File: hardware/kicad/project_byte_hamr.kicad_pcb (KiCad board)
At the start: 4 copper layers, 125.5 x 80.3 mm, 95 parts, among them J2 Conn_01x13_Socket, J3 Bus_Apple_II_Card_Side, J4 CONN_02X03, U1 LFE5U-25F-6BG381C, U10 IS25LP128F-JBLE, U11 SN74LVC8T245, U12 SN74LVC8T245, U13 SN74LVC8T245, U14 SN74LVC8T245, U2 MT48LC16M16A2TG, U3 TLV62569DBV, U4 TLV62569DBV, U5 TLV62569DBV, U6 FT231XQ, U8 SN74LVC8T245, U9 SN74LVC8T245, Y1 FNETHE025

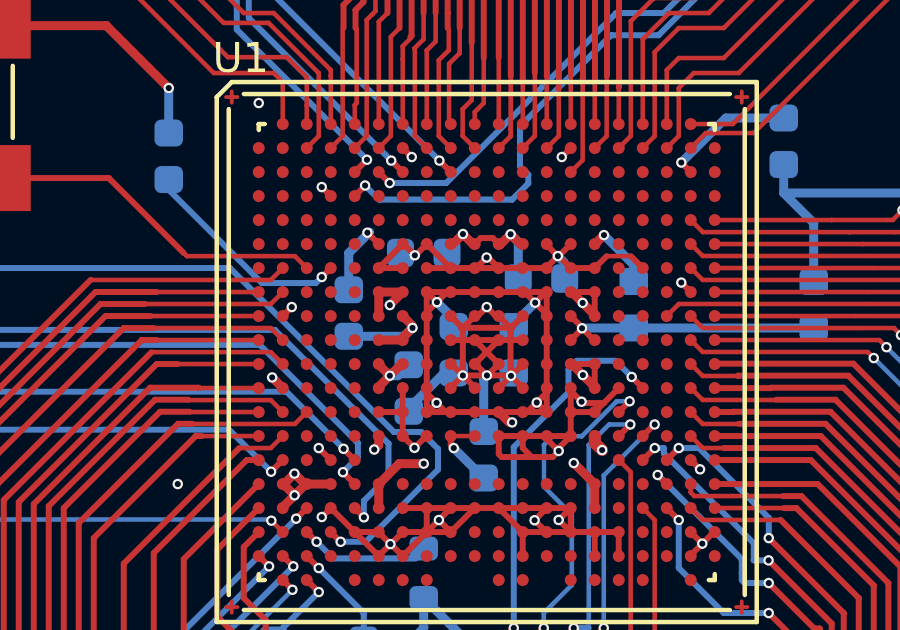
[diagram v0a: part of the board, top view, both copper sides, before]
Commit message: Update PCB design and replace outdated gerbers
Replaces old gerber files with a new version reflecting design
updates. Revamps PCB layout by adding new segments and vias while
removing outdated ones, optimizing net 2 connections for improved
efficiency and functionality. Corrects routing and aligns segments
with new design specifications.
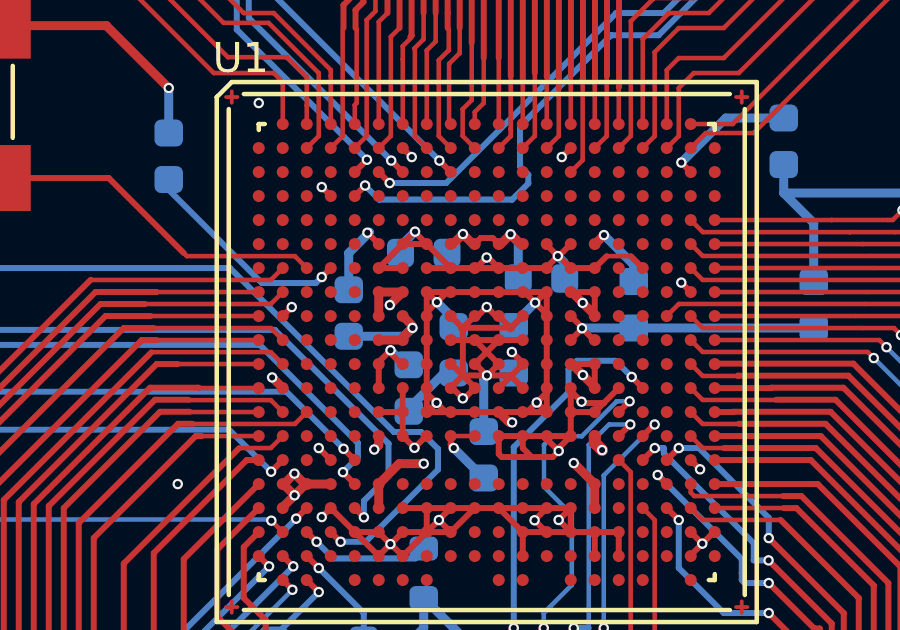
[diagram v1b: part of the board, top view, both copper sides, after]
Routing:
- net GND: track 412.0 -> 413.4 mm
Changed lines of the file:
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@@
 	)
 	(segment
-		(start 86.702219 93.57687)
-		(end 86.702219 93.602219)
-		(width 0.2)
-		(layer "F.Cu")
-		(net 2)
-	)
-	(segment
 		(start 92.276615 96.023385)
 		(end 91.9 96.4)
@@
 	)
 	(segment
+		(start 86.3 93.2)
+		(end 87.1 93.2)
+		(width 0.2)
+		(layer "F.Cu")
+		(net 2)
+	)
+	(segment
 		(start 95.584444 94.484444)
 		(end 95.9 94.8)
@@
 	)
 	(segment
+		(start 88.302376 98.344317)
+		(end 88.355683 98.344317)
+		(width 0.2)
+		(layer "F.Cu")
+		(net 2)
+	)
+	(segment
 		(start 91.502513 102.397487)
 		(end 91.9 102)
@@
 	)
 	(segment
+		(start 88.355683 98.344317)
+		(end 88.7 98)
+		(width 0.2)
+		(layer "F.Cu")
+		(net 2)
+	)
+	(segment
 		(start 88.7 96.4)
 		(end 89.5 96.4)
@@
 	)
 	(segment
-		(start 86.702219 93.57687)
-		(end 86.72313 93.57687)
-		(width 0.2)
-		(layer "F.Cu")
-		(net 2)
-	)
-	(segment
 		(start 98.2 123.65)
 		(end 98.2 122.4)
@@
 	)
 	(segment
-		(start 86.325349 93.2)
-		(end 86.702219 93.57687)
-		(width 0.2)
-		(layer "F.Cu")
-		(net 2)
-	)
-	(segment
 		(start 118.59908 86.05)
 		(end 118.59908 86.6)
@@
 	)
 	(segment
-		(start 86.3 93.2)
-		(end 86.325349 93.2)
-		(width 0.2)
-		(layer "F.Cu")
-		(net 2)
-	)
-	(segment
 		(start 117.1637 121)
 		(end 115.5 121)
@@
 	)
 	(segment
-		(start 89.892595 97.577637)
-		(end 89.892595 95.992595)
-		(width 0.2)
-		(layer "F.Cu")
-		(net 2)
-	)
-	(segment
 		(start 107.1 121.793)
 		(end 107.207 121.793)
@@
 	)
 	(segment
-		(start 86.72313 93.57687)
-		(end 87.1 93.2)
-		(width 0.2)
-		(layer "F.Cu")
-		(net 2)
-	)
-	(segment
 		(start 53.75 67.75)
 		(end 53.75 53.75)
@@
 	)
 	(segment
+		(start 90.3 97.2)
+		(end 90.3 97.162572)
+		(width 0.1525)
+		(layer "F.Cu")
+		(net 2)
+	)
+	(segment
 		(start 53.95 100.5)
 		(end 53.95 98.6125)
@@
 	)
 	(segment
+		(start 86.710035 92.786118)
+		(end 86.710035 92.810035)
+		(width 0.2)
+		(layer "F.Cu")
+		(net 2)
+	)
+	(segment
 		(start 87 117.85)
 		(end 91.0943 117.85)
@@
 	)
 	(segment
+		(start 90.3 97.162572)
+		(end 89.936933 96.799505)
+		(width 0.2)
+		(layer "F.Cu")
+		(net 2)
+	)
+	(segment
 		(start 85.5 96.4)
 		(end 86.3 96.4)
@@
 	)
 	(segment
+		(start 86.710035 92.810035)
+		(end 87.1 93.2)
+		(width 0.2)
+		(layer "F.Cu")
+		(net 2)
+	)
+	(segment
 		(start 91.1 99.700648)
 		(end 91.497687 100.098335)
@@
 	)
 	(segment
+		(start 87.9 98)
+		(end 87.958059 98)
+		(width 0.2)
+		(layer "F.Cu")
+		(net 2)
+	)
+	(segment
 		(start 88.7 97.2)
 		(end 88.72459 97.2)
@@
 	)
 	(segment
+		(start 86.3 93.196153)
+		(end 86.710035 92.786118)
+		(width 0.2)
+		(layer "F.Cu")
+		(net 2)
+	)
+	(segment
 		(start 91.1 93.970887)
 		(end 91.469233 93.601654)
@@
 	)
 	(segment
+		(start 87.958059 98)
+		(end 88.302376 98.344317)
+		(width 0.2)
+		(layer "F.Cu")
+		(net 2)
+	)
+	(segment
 		(start 59 94.5)
 		(end 59.5 94.5)
@@
 		(net 2)
 	)
+	(segment
+		(start 86.3 93.2)
+		(end 86.3 93.196153)
+		(width 0.2)
+		(layer "F.Cu")
+		(net 2)
+	)
 	(via
 		(at 83.6 102.3)
@@
 	)
 	(via
-		(at 89.90765 97.592692)
+		(at 89.936933 96.799505)
 		(size 0.35)
 		(drill 0.2)
@@
 	)
 	(via
-		(at 88.303495 97.580983)
+		(at 88.302376 98.344317)
 		(size 0.35)
 		(drill 0.2)
@@
 	)
 	(via
-		(at 86.702219 93.57687)
+		(at 86.710035 92.786118)
 		(size 0.35)
 		(drill 0.2)
@@
 	)
 	(segment
+		(start 86.225 93.5)
+		(end 86.225 93.271153)
+		(width 0.2)
+		(layer "B.Cu")
+		(net 2)
+	)
+	(segment
 		(start 84.5 96.275)
 		(end 86.344271 96.275)
@@
 	)
 	(segment
+		(start 86.225 93.271153)
+		(end 86.710035 92.786118)
+		(width 0.3)
+		(layer "B.Cu")
+		(net 2)
+	)
+	(segment
 		(start 91.70007 93.832491)
 		(end 91.469233 93.601654)
@@
 	)
 	(segment
-		(start 86.702219 93.57687)
-		(end 86.30187 93.57687)
-		(width 0.3)
-		(layer "B.Cu")
-		(net 2)
-	)
-	(segment
 		(start 84.7 83.8)
 		(end 82.168755 83.8)
@@
 	)
 	(segment
-		(start 86.258528 97.2)
-		(end 85.86936 97.589168)
-		(width 0.3)
-		(layer "F.Cu")
-		(net 9)
-	)
-	(segment
 		(start 94.8 83.8)
 		(end 94.8 84.49362)
@@
 	)
 	(segment
-		(start 85.5 97.2)
-		(end 85.5 97.219808)
-		(width 0.2)
-		(layer "F.Cu")
-		(net 9)
-	)
-	(segment
 		(start 62.5 93.85)
 		(end 61 93.85)
@@
 	)
 	(segment
-		(start 66.795 87.725)
-		(end 68.6 85.92)
-		(width 0.3)
+		(start 85.891559 96.740653)
+		(end 85.891559 96.833031)
+		(width 0.2)
 		(layer "F.Cu")
 		(net 9)
 	)
 	(segment
-		(start 83.037378 101.2)
-		(end 82.689278 100.8519)
+		(start 66.795 87.725)
+		(end 68.6 85.92)
 		(width 0.3)
 		(layer "F.Cu")
@@
 	)
 	(segment
-		(start 85.5 97.219808)
-		(end 85.86936 97.589168)
+		(start 83.037378 101.2)
+		(end 82.689278 100.8519)
 		(width 0.3)
 		(layer "F.Cu")
@@
 	)
 	(segment
-		(start 85.5 97.958528)
-		(end 85.86936 97.589168)
-		(width 0.3)
-		(layer "F.Cu")
-		(net 9)
-	)
-	(segment
 		(start 91.9 97.2)
 		(end 91.936996 97.2)
@@
 	)
 	(segment
+		(start 85.5 97.2)
+		(end 85.5 97.132212)
+		(width 0.2)
+		(layer "F.Cu")
+		(net 9)
+	)
+	(segment
 		(start 88.7 99.6)
 		(end 87.9 99.6)
@@
 	)
 	(segment
+		(start 85.891559 96.833031)
+		(end 86.258528 97.2)
+		(width 0.2)
+		(layer "F.Cu")
+		(net 9)
+	)
+	(segment
+		(start 85.5 98)
+		(end 85.5 97.2)
+		(width 0.2)
+		(layer "F.Cu")
+		(net 9)
+	)
+	(segment
 		(start 113.26658 85.5675)
 		(end 113.29908 85.6)
@@
 	)
 	(segment
-		(start 85.5 98)
-		(end 85.5 97.958528)
-		(width 0.2)
-		(layer "F.Cu")
-		(net 9)
-	)
-	(segment
 		(start 83.9 101.2)
 		(end 83.1 101.2)
@@
 	)
 	(segment
+		(start 85.5 97.132212)
+		(end 85.891559 96.740653)
+		(width 0.2)
+		(layer "F.Cu")
+		(net 9)
+	)
+	(segment
 		(start 89.5 115.3)
 		(end 89.2 115)
@@
 	)
 	(via
-		(at 85.86936 97.589168)
-		(size 0.35)
-		(drill 0.2)
-		(layers "F.Cu" "B.Cu")
-		(free yes)
-		(net 9)
-	)
-	(via
 		(at 82.689278 100.8519)
 		(size 0.35)
@@
 	)
 	(via
+		(at 85.891559 96.740653)
+		(size 0.35)
+		(drill 0.2)
+		(layers "F.Cu" "B.Cu")
+		(net 9)
+	)
+	(via
 		(at 78.5 88)
 		(size 0.35)
@@
 	)
 	(segment
+		(start 86.375906 97.225)
+		(end 85.891559 96.740653)
+		(width 0.3)
+		(layer "B.Cu")
+		(net 9)
+	)
+	(segment
 		(start 85.5 75.5)
 		(end 85 75)
@@
 	)
 	(segment
-		(start 86.135832 97.589168)
-		(end 86.5 97.225)
-		(width 0.3)
-		(layer "B.Cu")
-		(net 9)
-	)
-	(segment
 		(start 89 101)
 		(end 88 100)
@@
 	)
 	(segment
+		(start 86.5 97.225)
+		(end 86.375906 97.225)
+		(width 0.2)
+		(layer "B.Cu")
+		(net 9)
+	)
+	(segment
 		(start 85 75)
 		(end 82.10458 75)
@@
 	)
 	(segment
-		(start 85.86936 97.589168)
-		(end 86.135832 97.589168)
-		(width 0.3)
-		(layer "B.Cu")
-		(net 9)
-	)
-	(segment
 		(start 78.5 89.5)
 		(end 78.5 88)
@@
 	)
 	(segment
+		(start 85.86936 97)
+		(end 85.86936 95.23577)
+		(width 0.4)
+		(layer "In2.Cu")
+		(net 9)
+	)
+	(segment
 		(start 84 75)
 		(end 84 80)
@@
 	(segment
 		(start 85.86936 97.589168)
-		(end 85.86936 95.23577)
+		(end 85.86936 97)
 		(width 0.4)
 		(layer "In2.Cu")

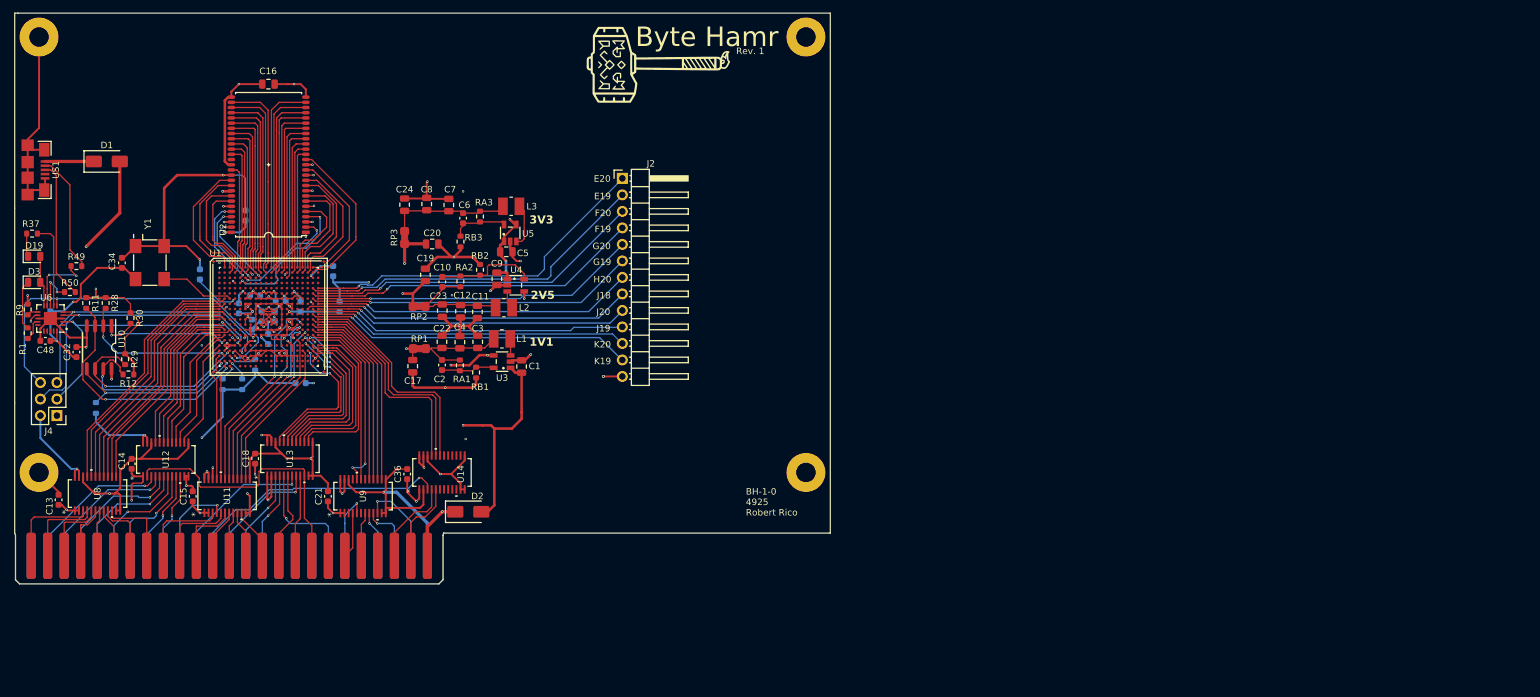
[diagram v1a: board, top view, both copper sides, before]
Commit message: Redesign 1.1
A complete redesign. Physical constraints were not meant.
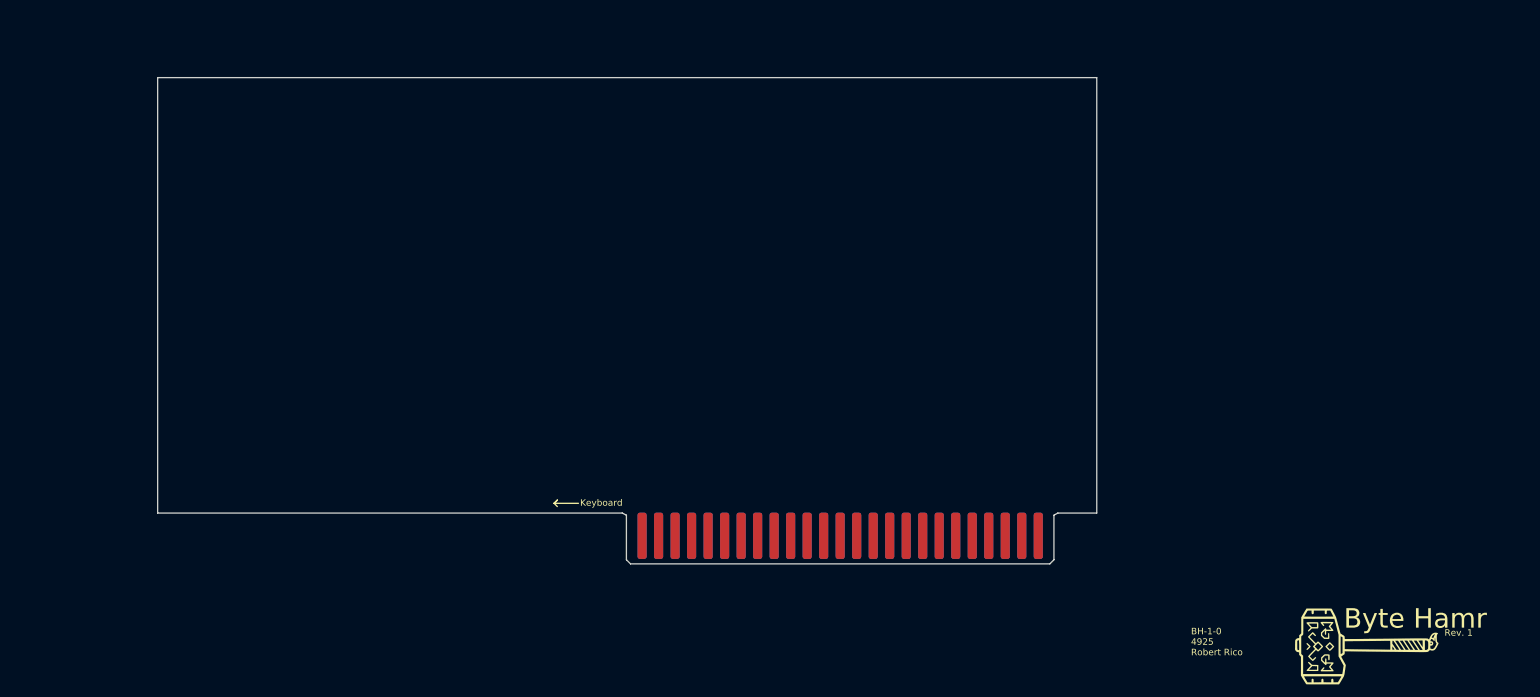
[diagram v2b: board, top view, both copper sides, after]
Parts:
- removed C1, C11, C12, C3, C4, C5, C7, C8, C9: 22uF, Capacitor_SMD:C_0805_2012Metric
- removed C10, C2, C6: 100pF, Capacitor_SMD:C_0603_1608Metric
- removed C13, C14, C15, C18, C21, C25, C26, C27, C28, C29, C30, C31, C32, C33, C34, C35, C36, C48, C49, C50, C51, C52, C53: 22nF, Capacitor_SMD:C_0603_1608Metric
- removed C16, C17, C19, C20, C22, C23, C24: 2.2uF, Capacitor_SMD:C_0805_2012Metric
- removed D1, D2: STPS2L40AF, Diode_SMD:D_SMA
- removed D19: RED, LED_SMD:LED_0805_2012Metric
- removed D3: YELLOW, LED_SMD:LED_0805_2012Metric
- removed H1, H2, H3, H4: MountingHole_Pad, MountingHole:MountingHole_3mm_Pad
- removed J2: Conn_01x13_Socket, Connector_PinHeader_2.54mm:PinHeader_1x13_P2.54mm_Horizontal
- removed J4: CONN_02X03, Connector_PinHeader_2.54mm:PinHeader_2x03_P2.54mm_Vertical
- removed L1, L2, L3: 2.2uH, L_1008_1210:L_1008_1210
- removed R1, R37: 549, Resistor_SMD:R_0603_1608Metric
- removed R11, R12, R27, R28: 10k, Resistor_SMD:R_0603_1608Metric
- removed R29: 1.1k, Resistor_SMD:R_0603_1608Metric
- removed R30, RB2: 4.7k, Resistor_SMD:R_0603_1608Metric
- removed R31, R32, R33, R9, RA1, RA2, RA3: 15k, Resistor_SMD:R_0603_1608Metric
- removed R49, R50: 27, Resistor_SMD:R_0603_1608Metric
- removed RB1: 18k, Resistor_SMD:R_0603_1608Metric
- removed RB3: 3.3k, Resistor_SMD:R_0603_1608Metric
- removed RP1, RP2, RP3: 0, jumper:R_0805_2012Metric_Pad1.29x1.40mm_HandSolder_Jumper_NC
- removed U1: LFE5U-25F-6BG381C, lfe5bg381:BGA-381_pitch0.8mm_dia0.4mm
- removed U10: IS25LP128F-JBLE, SOA008-150mil:SOA008-150-208mil
- removed U11, U12, U13, U14, U8, U9: SN74LVC8T245, footprints:DBQ24-L
- removed U2: MT48LC16M16A2TG, TSOP54:TSOP54
- removed U3, U4, U5: TLV62569DBV, TSOT-25:TSOT-25
- removed U6: FT231XQ, ft231x:FT231X-QFN-20-1EP_4x4mm_P0.5mm_EP2x2mm
- removed US1: MICRO_USB, usb_otg:USB-MICRO-B-FCI-10118192-0001LF
- removed Y1: FNETHE025, oscxo:Crystal_SMD_7050_4Pads
- moved G*** 141.0 mm to (258.0, 147.5)
- moved J3 94.1 mm to (177.0, 130.5)
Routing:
- net GND: track 413.4 -> 0.00 mm, vias 52 -> 0
- net +3V3: track 378.3 -> 0.00 mm, vias 33 -> 0
- net +5V: track 109.8 -> 0.00 mm, vias 11 -> 0
- net CARD5V: track 60.5 -> 0.00 mm, vias 8 -> 0
- net +1V1: track 59.5 -> 0.00 mm, vias 8 -> 0
- net JTAG_TDO: track 58.3 -> 0.00 mm, vias 2 -> 0
- net I/O_PIN_12: track 55.0 -> 0.00 mm, vias 1 -> 0
- net I/O_PIN_11: track 54.7 -> 0.00 mm, vias 1 -> 0
- net +2V5: track 52.6 -> 0.00 mm, vias 5 -> 0
- net I/O_PIN_9: track 52.1 -> 0.00 mm, vias 1 -> 0
- net I/O_PIN_10: track 52.0 -> 0.00 mm, vias 1 -> 0
- net I/O_PIN_5: track 50.8 -> 0.00 mm, vias 1 -> 0
- net I/O_PIN_1: track 50.5 -> 0.00 mm, vias 1 -> 0
- net I/O_PIN_7: track 50.5 -> 0.00 mm, vias 1 -> 0
- net I/O_PIN_8: track 50.2 -> 0.00 mm, vias 1 -> 0
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- removed copper zone on In2.Cu, net +3V3
- removed copper zone on In2.Cu, net +5V
- removed copper zone on In2.Cu, net CARD5V
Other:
- board size 125.5 x 80.3 mm -> 144.5 x 67.3 mm
- board text added: "Keyboard"
- board text removed: "1V1"
- board text removed: "2V5"
- board text removed: "3V3"
- board text removed: "E19"
- board text removed: "E20"
- board text removed: "F19"
- board text removed: "F20"
- board text removed: "G19"
- board text removed: "G20"
- board text removed: "H20"
- board text removed: "J18"
- board text removed: "J19"
- board text removed: "J20"
- board text removed: "K19"
- board text removed: "K20"
